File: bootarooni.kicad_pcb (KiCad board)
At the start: 2 copper layers, 32 parts, among them J1 USB_B_Micro, U1 74LS05, U2 Pico_USB, U3 ADUM3160, U4 74LCX541, U5 74AHCT1G125, U6 74LS299, U7 74LS299, U8 74LS299

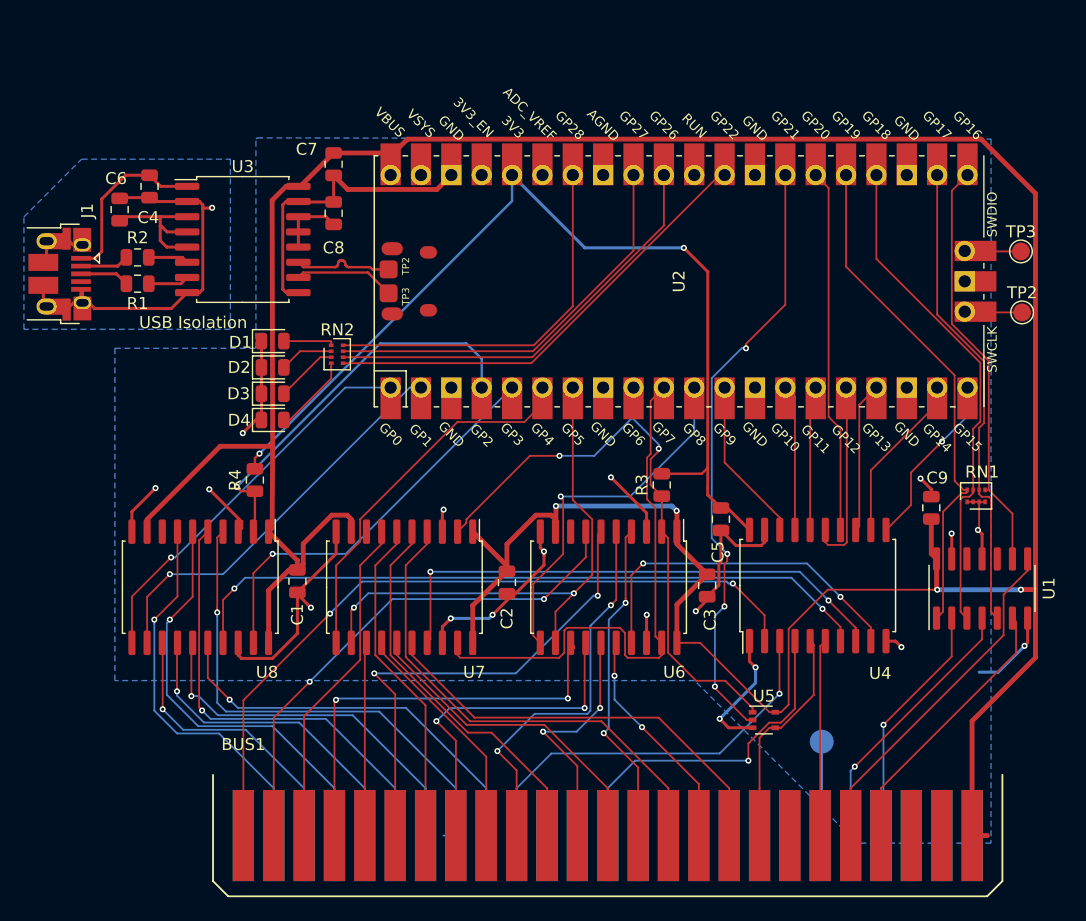
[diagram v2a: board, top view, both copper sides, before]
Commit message: added mounting holes, board outlines
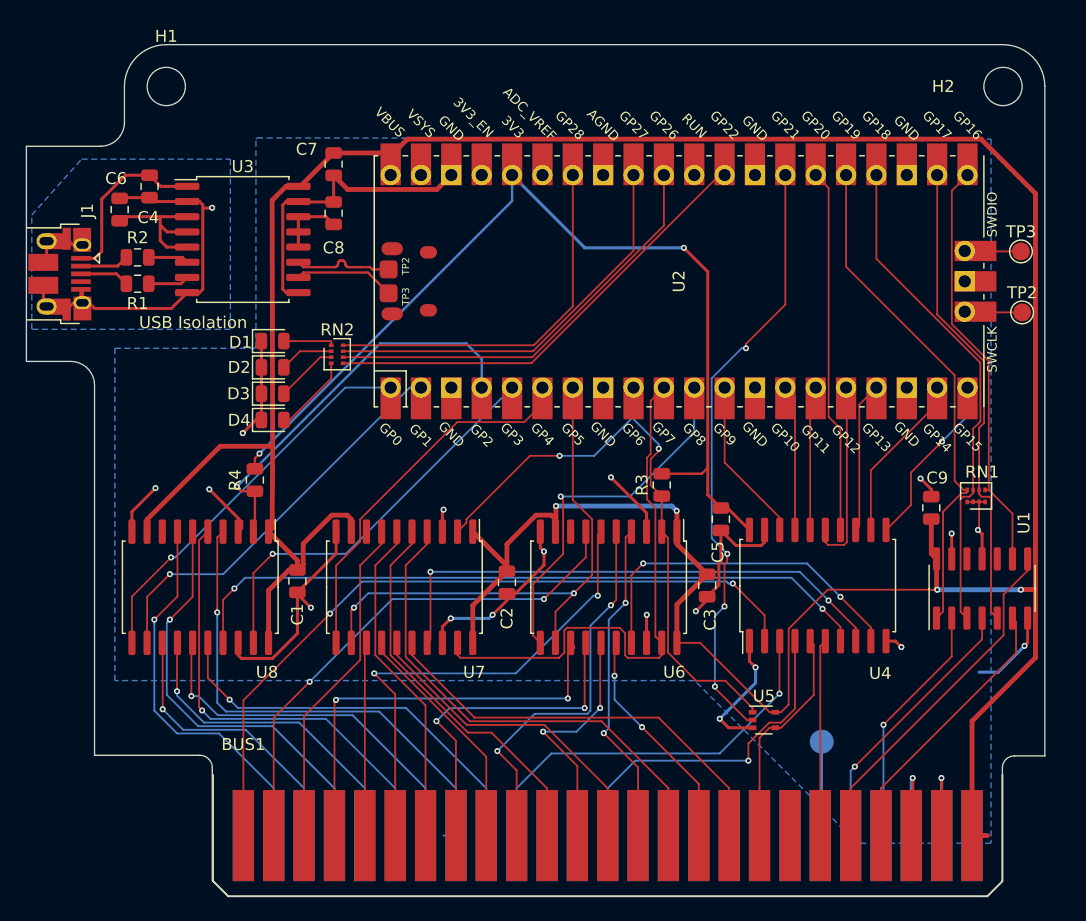
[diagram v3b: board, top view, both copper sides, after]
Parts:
- added H1: top mount, MountingHole:MountingHole_3.2mm_M3, F.Cu at (97.0, 47.0)
- added H2: top mount, MountingHole:MountingHole_3.2mm_M3, F.Cu at (167.0, 47.0)
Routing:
- net Net-(BUS1-Pad23): track 0.00 -> 9.73 mm, vias 0 -> 1
- net Net-(BUS1-Pad24): track 0.00 -> 9.65 mm, vias 0 -> 1
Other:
- board outline added: 85.2 x 71.2 mm
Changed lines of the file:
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@@
   (general
     (thickness 1.6)
-    (drawings 1)
-    (tracks 786)
+    (drawings 21)
+    (tracks 796)
     (zones 0)
-    (modules 32)
+    (modules 34)
     (nets 105)
   )
@@
     (uvia_drill 0.1)
   )
+  (module MountingHole:MountingHole_3.2mm_M3 (layer F.Cu)
+    (at 167 47)
+    (descr "Mounting Hole 3.2mm, no annular, M3")
+    (tags "mounting hole 3.2mm no annular m3")
+    (attr virtual)
+    (fp_text reference H2 (at -5 0) (layer F.SilkS)
+      (effects (font (size 1 1) (thickness 0.15)))
+    )
+    (fp_text value "top mount" (at 0 4.2) (layer F.Fab)
+      (effects (font (size 1 1) (thickness 0.15)))
+    )
+    (fp_circle (center 0 0) (end 3.45 0) (layer F.CrtYd) (width 0.05))
+    (fp_circle (center 0 0) (end 3.2 0) (layer Cmts.User) (width 0.15))
+    (fp_text user %R (at 0.3 0) (layer F.Fab)
+      (effects (font (size 1 1) (thickness 0.15)))
+    )
+    (pad 1 np_thru_hole circle (at 0 0) (size 3.2 3.2) (drill 3.2) (layers *.Cu *.Mask))
+  )
+  (module MountingHole:MountingHole_3.2mm_M3 (layer F.Cu)
+    (at 97 47)
+    (descr "Mounting Hole 3.2mm, no annular, M3")
+    (tags "mounting hole 3.2mm no annular m3")
+    (attr virtual)
+    (fp_text reference H1 (at 0 -4.2) (layer F.SilkS)
+      (effects (font (size 1 1) (thickness 0.15)))
+    )
+    (fp_text value "top mount" (at 0 4.2) (layer F.Fab)
+      (effects (font (size 1 1) (thickness 0.15)))
+    )
+    (fp_circle (center 0 0) (end 3.45 0) (layer F.CrtYd) (width 0.05))
+    (fp_circle (center 0 0) (end 3.2 0) (layer Cmts.User) (width 0.15))
+    (fp_text user %R (at 0.3 0) (layer F.Fab)
+      (effects (font (size 1 1) (thickness 0.15)))
+    )
+    (pad 1 np_thru_hole circle (at 0 0) (size 3.2 3.2) (drill 3.2) (layers *.Cu *.Mask))
+  )
   (module Package_SO:SOIC-20W_7.5x12.8mm_P1.27mm (layer F.Cu)
     (at 134.005 88.892 270)
@@
     (tags "SOIC SO")
     (attr smd)
-    (fp_text reference U1 (at 0 5.6 90) (layer F.SilkS)
+    (fp_text reference U1 (at 5.5 3.5 90) (layer F.SilkS)
       (effects (font (size 1 1) (thickness 0.15)))
     )
@@
     )
   )
+  (gr_line (start 99.8 102.95) (end 91 102.95) (layer Edge.Cuts) (width 0.05))
+  (gr_arc (start 99.8 104) (end 100.85 104) (angle -90) (layer Edge.Cuts) (width 0.05))
+  (gr_line (start 100.85 113.4) (end 100.85 104) (layer Edge.Cuts) (width 0.05))
+  (gr_line (start 102.2 114.75) (end 100.85 113.4) (layer Edge.Cuts) (width 0.05))
+  (gr_line (start 165.7 114.75) (end 102.2 114.75) (layer Edge.Cuts) (width 0.05))
+  (gr_line (start 91 72) (end 91 102.95) (layer Edge.Cuts) (width 0.05))
+  (gr_arc (start 89 72) (end 91 72) (angle -90) (layer Edge.Cuts) (width 0.05))
+  (gr_line (start 85.3 70) (end 89 70) (layer Edge.Cuts) (width 0.05))
+  (gr_line (start 85.3 52) (end 85.3 70) (layer Edge.Cuts) (width 0.05))
+  (gr_line (start 91.5 52) (end 85.3 52) (layer Edge.Cuts) (width 0.05))
+  (gr_arc (start 91.5 50) (end 91.5 52) (angle -90) (layer Edge.Cuts) (width 0.05))
+  (gr_line (start 93.5 47) (end 93.5 50) (layer Edge.Cuts) (width 0.05))
+  (gr_arc (start 97 47) (end 97 43.5) (angle -90) (layer Edge.Cuts) (width 0.05))
+  (gr_line (start 167 43.5) (end 97 43.5) (layer Edge.Cuts) (width 0.05))
+  (gr_arc (start 167 47) (end 170.5 47) (angle -90) (layer Edge.Cuts) (width 0.05))
+  (gr_line (start 170.5 103) (end 170.5 47) (layer Edge.Cuts) (width 0.05))
+  (gr_line (start 167.95 103) (end 170.5 103) (layer Edge.Cuts) (width 0.05))
+  (gr_arc (start 167.95 104) (end 167.95 103) (angle -90) (layer Edge.Cuts) (width 0.05))
+  (gr_line (start 166.95 113.5) (end 166.95 104) (layer Edge.Cuts) (width 0.05))
+  (gr_line (start 165.7 114.75) (end 166.95 113.5) (layer Edge.Cuts) (width 0.05))
   (gr_text "USB Isolation\n" (at 99.25 66.75) (layer F.SilkS)
     (effects (font (size 1 1) (thickness 0.15)))
@@
   (segment (start 168.09 91.775) (end 168.09 94.405602) (width 0.1524) (layer F.Cu) (net 22))
   (segment (start 167.79 91.475) (end 168.09 91.775) (width 0.1524) (layer F.Cu) (net 22))
+  (via (at 159.45 104.85) (size 0.508) (drill 0.254) (layers F.Cu B.Cu) (net 23))
+  (segment (start 159.331001 104.968999) (end 159.45 104.85) (width 0.254) (layer B.Cu) (net 23))
+  (segment (start 159.331001 109.667001) (end 159.331001 104.968999) (width 0.254) (layer B.Cu) (net 23))
+  (segment (start 159.45 109.548002) (end 159.331001 109.667001) (width 0.254) (layer F.Cu) (net 23))
+  (segment (start 159.45 104.85) (end 159.45 109.548002) (width 0.254) (layer F.Cu) (net 23))
+  (via (at 161.85 104.85) (size 0.508) (drill 0.254) (layers F.Cu B.Cu) (net 24))
+  (segment (start 161.871001 104.871001) (end 161.85 104.85) (width 0.254) (layer F.Cu) (net 24))
+  (segment (start 161.871001 109.667001) (end 161.871001 104.871001) (width 0.254) (layer F.Cu) (net 24))
+  (segment (start 161.85 109.646) (end 161.871001 109.667001) (width 0.254) (layer B.Cu) (net 24))
+  (segment (start 161.85 104.85) (end 161.85 109.646) (width 0.254) (layer B.Cu) (net 24))
   (segment (start 108.05 55.355) (end 108.155 55.355) (width 0.254) (layer F.Cu) (net 25))
   (segment (start 164.411001 106.606999) (end 164.592 106.426) (width 0.4064) (layer F.Cu) (net 25))
@@
     (polygon
       (pts
-        (xy 102.362 67.31) (xy 85.09 67.31) (xy 85.09 57.912) (xy 89.916 53.086) (xy 102.362 53.086)
+        (xy 102.362 67.31) (xy 85.75 67.31) (xy 85.75 57.75) (xy 89.916 53.086) (xy 102.362 53.086)
       )
     )

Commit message: final v1; board, digikey, and stencil orders submitted
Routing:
- net +5V: track 284.6 -> 283.3 mm
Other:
- board text added: "ADDR EVEN"
- board text added: "ADDR ODD"
- board text added: "DATA"
- board text added: "Multipurpose Pico ][e, revision 1"
- board text added: "REAR"
- board text added: "phooky/2021"
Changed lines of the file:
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@@
   (general
     (thickness 1.6)
-    (drawings 21)
-    (tracks 796)
+    (drawings 27)
+    (tracks 795)
     (zones 0)
     (modules 34)
@@
     (visible_elements FFFFFF7F)
     (pcbplotparams
-      (layerselection 0x010fc_ffffffff)
+      (layerselection 0x01008_7ffffffe)
       (usegerberextensions false)
       (usegerberattributes false)
@@
       (outputformat 1)
       (mirror false)
-      (drillshape 1)
+      (drillshape 0)
       (scaleselection 1)
       (outputdirectory ""))
@@
     (descr "Through hole straight pin header, 2x20, 2.54mm pitch, double rows")
     (tags "Through hole pin header THT 2x20 2.54mm double row")
-    (fp_text reference U2 (at 0 0 270) (layer F.SilkS)
+    (fp_text reference U2 (at -9 26.9 270) (layer F.SilkS)
       (effects (font (size 1 1) (thickness 0.15)))
     )
@@
       (rotate (xyz 0 0 0))
     )
+  )
+  (gr_text phooky/2021 (at 149.6 45.7) (layer F.SilkS)
+    (effects (font (size 1.524 1.524) (thickness 0.1524)))
+  )
+  (gr_text REAR (at 168.3 77 90) (layer F.SilkS)
+    (effects (font (size 1.524 1.524) (thickness 0.15) italic))
+  )
+  (gr_text "ADDR EVEN" (at 134 96.4) (layer F.SilkS)
+    (effects (font (size 1.524 1.524) (thickness 0.15) italic))
+  )
+  (gr_text "ADDR ODD" (at 116.6 96.5) (layer F.SilkS)
+    (effects (font (size 1.524 1.524) (thickness 0.15) italic))
+  )
+  (gr_text DATA (at 95.4 96.5) (layer F.SilkS)
+    (effects (font (size 1.524 1.524) (thickness 0.15) italic))
+  )
+  (gr_text "Multipurpose Pico ][e, revision 1" (at 120.4 45.8) (layer F.Cu)
+    (effects (font (size 1.5 1.5) (thickness 0.3)))
   )
   (gr_line (start 99.8 102.95) (end 91 102.95) (layer Edge.Cuts) (width 0.05))
@@
   (segment (start 164.411001 106.606999) (end 164.592 106.426) (width 0.4064) (layer F.Cu) (net 25))
   (segment (start 164.411001 109.667001) (end 164.411001 106.606999) (width 0.4064) (layer F.Cu) (net 25))
-  (segment (start 164.411001 109.667001) (end 165.706401 109.667001) (width 0.4064) (layer F.Cu) (net 25))
   (segment (start 161 86.085) (end 161.44 86.525) (width 0.4064) (layer F.Cu) (net 25))
   (segment (start 161 83.1875) (end 161 86.085) (width 0.4064) (layer F.Cu) (net 25))
